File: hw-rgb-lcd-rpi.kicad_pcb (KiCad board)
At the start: 2 copper layers, 14 parts, among them J1 lq043t1dg03, J2 minilaptop-lcd, P1 GPIO, P2 I2C, P3 BATT, P4 MINILAP SPARE, P5 P_LED, P6 BACKLIGHT, U1 RPi_A+_B+_2B_Hat

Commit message: Set design rules as per hackvana
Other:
- net class Default: clearance 0.2 -> 0.1524; trace_width 0.25 -> 0.1524
- rule trace_clearance: 0.2 -> 0.1524
- rule trace_min: 0.2 -> 0.1524
- rule via_min_size: 0.4 -> 0.6
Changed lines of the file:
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@@
   )
   (setup
-    (last_trace_width 0.25)
-    (trace_clearance 0.2)
+    (last_trace_width 0.1524)
+    (trace_clearance 0.1524)
     (zone_clearance 0.508)
     (zone_45_only no)
-    (trace_min 0.2)
+    (trace_min 0.1524)
     (segment_width 0.2)
     (edge_width 0.15)
     (via_size 0.6)
     (via_drill 0.4)
-    (via_min_size 0.4)
+    (via_min_size 0.6)
     (via_min_drill 0.3)
     (uvia_size 0.3)
     (uvia_drill 0.1)
     (uvias_allowed no)
-    (uvia_min_size 0.2)
-    (uvia_min_drill 0.1)
+    (uvia_min_size 0)
+    (uvia_min_drill 0)
     (pcb_text_width 0.3)
     (pcb_text_size 1.5 1.5)
@@
     (pad_to_mask_clearance 0.2)
     (aux_axis_origin 0 0)
-    (visible_elements FFFFFF7F)
+    (visible_elements FFFFFFFF)
     (pcbplotparams
       (layerselection 0x00030_80000001)
@@
   (net 52 "Net-(P6-Pad3)")
   (net_class Default "This is the default net class."
-    (clearance 0.2)
-    (trace_width 0.25)
+    (clearance 0.1524)
+    (trace_width 0.1524)
     (via_dia 0.6)
     (via_drill 0.4)

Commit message: Make power tracks visibly wider
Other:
- net class Power added: clearance 0.2, trace_width 0.2, via_dia 0.6, via_drill 0.4
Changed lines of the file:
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@@
     (uvia_dia 0.3)
     (uvia_drill 0.1)
-    (add_net +BATT)
     (add_net /B0)
     (add_net /B1)
@@
     (add_net /SDA)
     (add_net /V_SYNC)
-    (add_net GND)
     (add_net "Net-(J1-Pad34)")
     (add_net "Net-(J1-Pad37)")
@@
     (add_net "Net-(J2-Pad14)")
     (add_net "Net-(J2-Pad9)")
+    (add_net "Net-(P6-Pad2)")
+    (add_net "Net-(P6-Pad3)")
+  )
+  (net_class Power ""
+    (clearance 0.2)
+    (trace_width 0.2)
+    (via_dia 0.6)
+    (via_drill 0.4)
+    (uvia_dia 0.3)
+    (uvia_drill 0.1)
+    (add_net +BATT)
+    (add_net GND)
     (add_net "Net-(JP4-Pad1)")
     (add_net "Net-(JP5-Pad2)")
-    (add_net "Net-(P6-Pad2)")
-    (add_net "Net-(P6-Pad3)")
     (add_net VCC)
   )

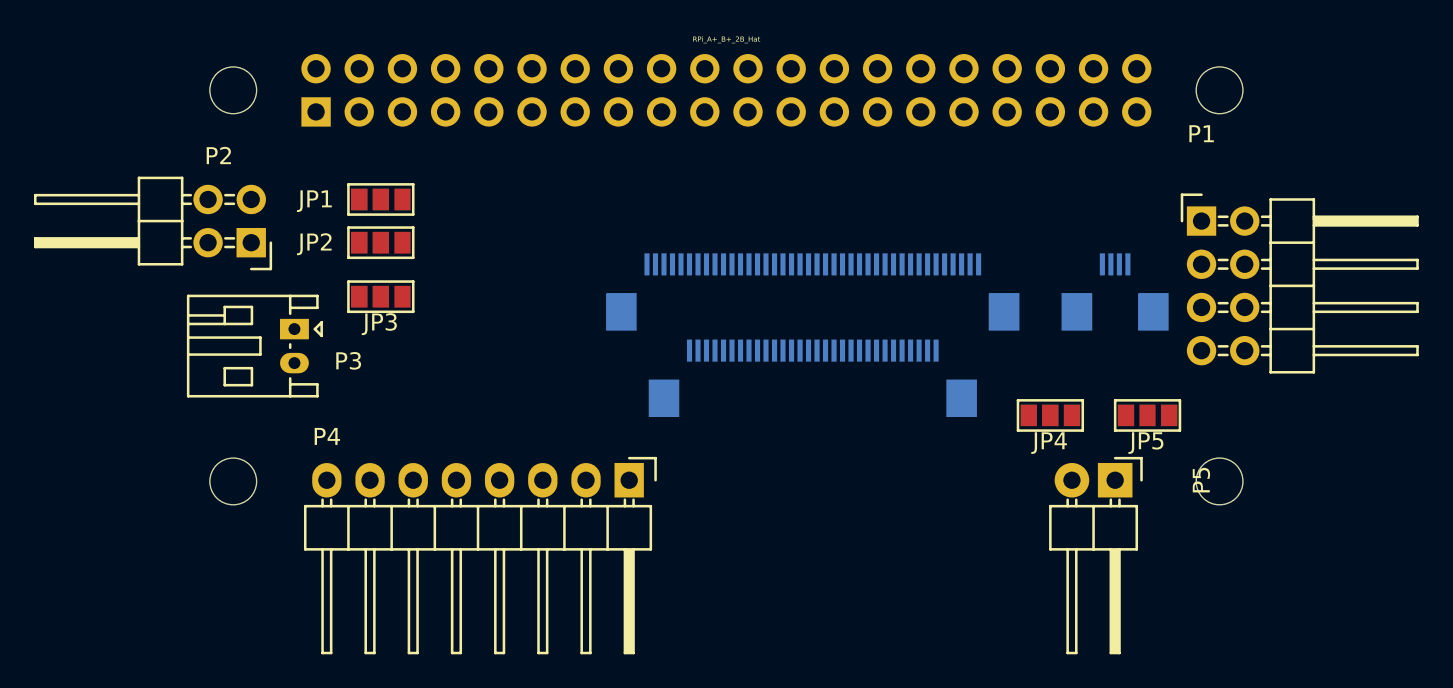
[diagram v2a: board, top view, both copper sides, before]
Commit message: All tracks routed, however the layout is sub-optimal
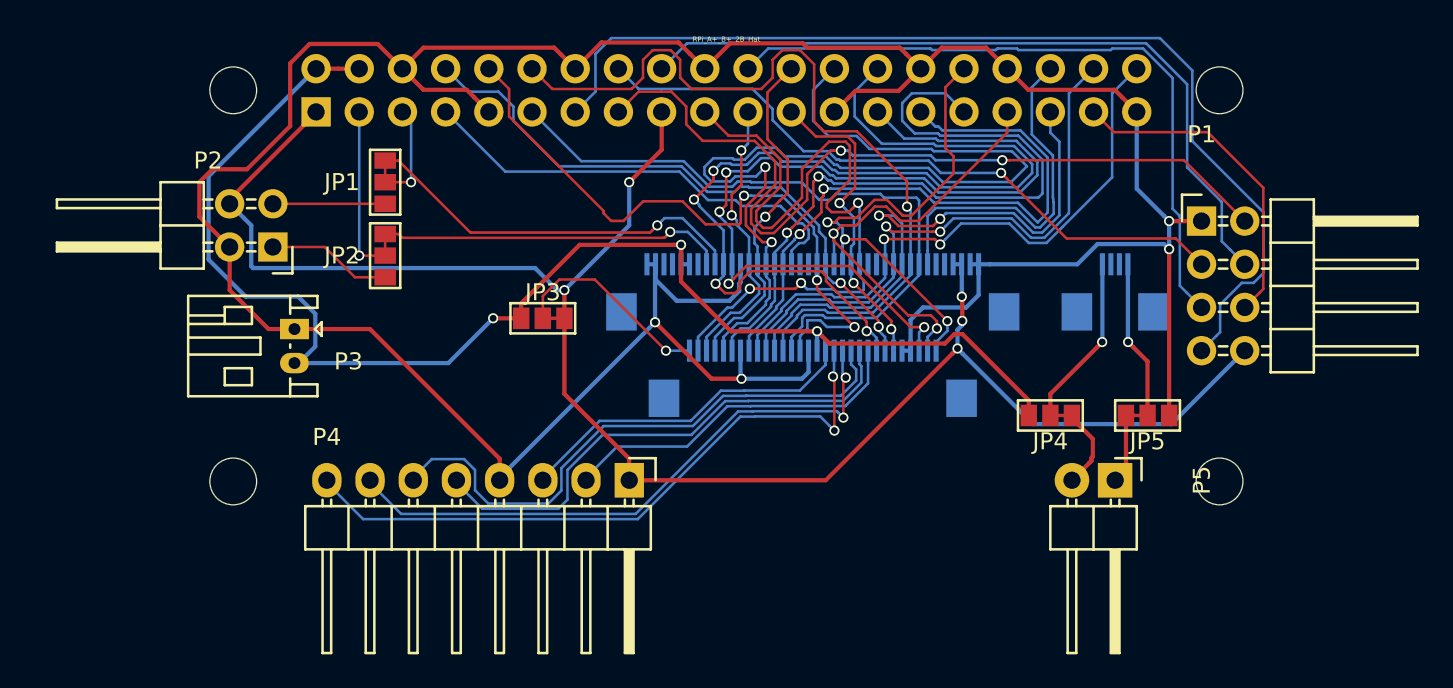
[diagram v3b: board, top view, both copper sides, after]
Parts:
- JP3: value J_VBATT -> 3v3_5v
- moved JP3 9.61 mm to (137.8, 107.3), turned to 90 degrees
- moved P2 1.30 mm to (121.9, 103.1)
- moved JP1 1.05 mm to (128.5, 99.3), turned to 180 degrees
- moved JP2 0.80 mm to (128.5, 103.6), turned to 0 degrees
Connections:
- J2 pad 30: +BATT -> Net-(J2-Pad30)
- JP3 pad 1: VCC -> +BATT
- JP3 pad 2: +BATT -> Net-(J2-Pad30)
- JP3 pad 3: +BATT -> VCC
- P2 pad 1: VCC -> /SDA
- P2 pad 2: /SDA -> GND
- P2 pad 4: GND -> VCC
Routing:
- net GND: track 0.00 -> 187.7 mm, vias 0 -> 4
- net VCC: track 0.00 -> 104.0 mm, vias 0 -> 5
- net +BATT: track 0.00 -> 83.3 mm, vias 0 -> 3
- net /GPIO27: track 0.00 -> 60.3 mm
- net /DEN: track 0.00 -> 57.3 mm, vias 0 -> 4
- net /B5: track 0.00 -> 56.4 mm, vias 0 -> 2
- net /DOTCLK: track 0.00 -> 53.3 mm, vias 0 -> 4
- net /GPIO22: track 0.00 -> 50.1 mm, vias 0 -> 2
- net /R4: track 0.00 -> 48.2 mm, vias 0 -> 1
- net /GPIO24: track 0.00 -> 44.5 mm
- net /B4: track 0.00 -> 43.0 mm, vias 0 -> 2
- net /G2: track 0.00 -> 42.5 mm, vias 0 -> 3
- net /GPIO25: track 0.00 -> 40.5 mm
- net /R3: track 0.00 -> 40.1 mm
- net /GPIO23: track 0.00 -> 39.4 mm, vias 0 -> 1
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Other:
- net class Power: trace_width 0.2 -> 0.25

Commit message: Rearrange the mini-laptop spare pins to make routing simple
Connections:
- P4 pad 3: Net-(J2-Pad14) -> Net-(J2-Pad10)
- P4 pad 4: GND -> Net-(J2-Pad11)
- P4 pad 5: Net-(J2-Pad10) -> Net-(J2-Pad12)
- P4 pad 6: Net-(J2-Pad11) -> Net-(J2-Pad13)
- P4 pad 7: Net-(J2-Pad12) -> Net-(J2-Pad14)
- P4 pad 8: Net-(J2-Pad13) -> GND
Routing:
- net GND: track 187.7 -> 168.1 mm
- net Net-(J2-Pad14): track 20.4 -> 32.9 mm
- net Net-(J2-Pad13): track 38.5 -> 30.0 mm, vias 2 -> 0
- net Net-(J2-Pad11): track 34.1 -> 25.9 mm
- net Net-(J2-Pad12): track 35.5 -> 28.1 mm, vias 2 -> 0
- net Net-(J2-Pad10): track 30.6 -> 23.8 mm
- net Net-(J2-Pad9): track 21.0 -> 21.7 mm

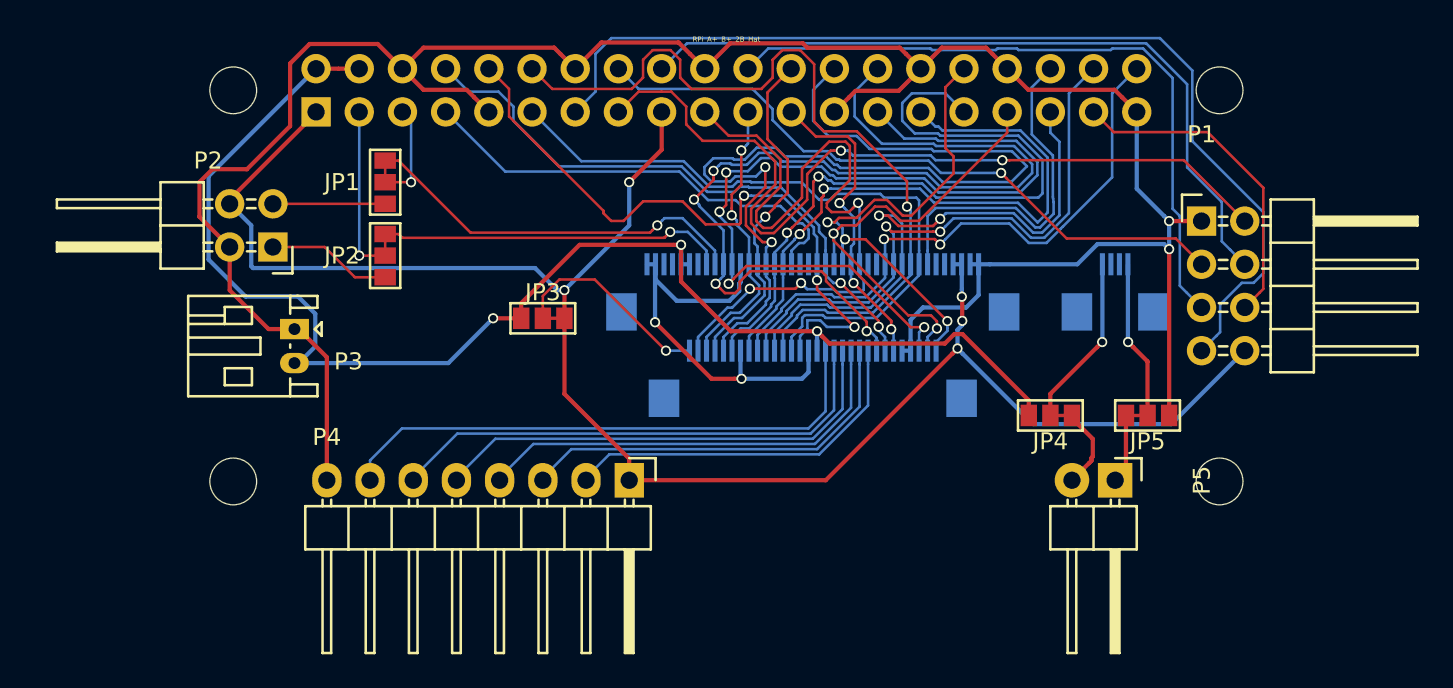
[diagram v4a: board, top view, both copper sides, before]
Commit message: Clean up routing
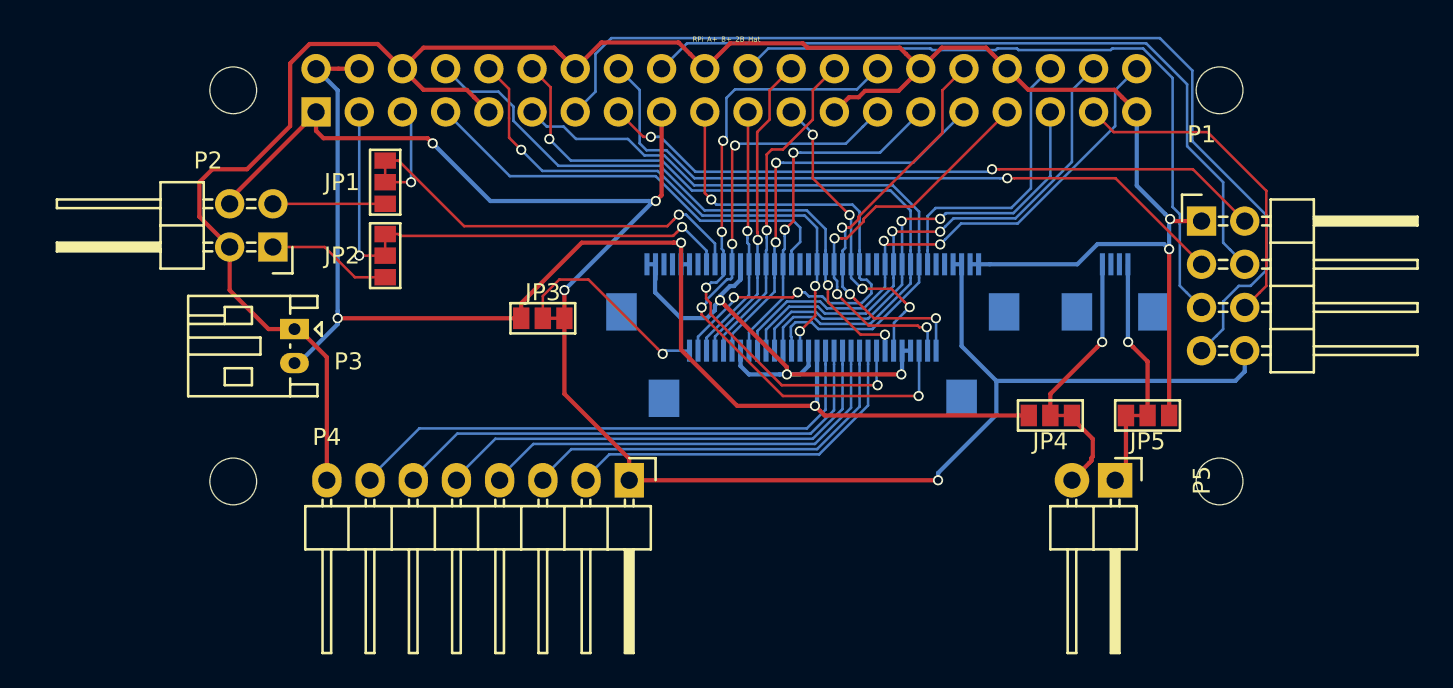
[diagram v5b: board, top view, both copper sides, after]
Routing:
- net /B5: track 56.4 -> 19.7 mm, vias 2 -> 1
- net /DEN: track 57.3 -> 37.0 mm
- net /B4: track 43.0 -> 24.4 mm
- net /B3: track 37.4 -> 21.2 mm
- net /DOTCLK: track 53.3 -> 37.5 mm
- net /GPIO22: track 50.1 -> 39.6 mm
- net /G2: track 42.5 -> 32.3 mm
- net /G4: track 30.9 -> 24.4 mm
- net /G7: track 38.9 -> 32.5 mm
- net /R4: track 48.2 -> 42.2 mm
- net +BATT: track 83.3 -> 77.5 mm
- net /R5: track 33.2 -> 27.6 mm
- net /R2: track 20.7 -> 17.1 mm
- net /R6: track 34.6 -> 31.6 mm
- net /G5: track 26.9 -> 24.2 mm, vias 2 -> 3
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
